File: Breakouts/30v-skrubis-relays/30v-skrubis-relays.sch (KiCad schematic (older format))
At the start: 13 parts, among them J1 Conn_01x03, J2 Conn_01x01, J4 Conn_01x01, J5 Conn_01x02, K1 G5Q-1A, Q1 Q_PNP_BEC, U1 PC817

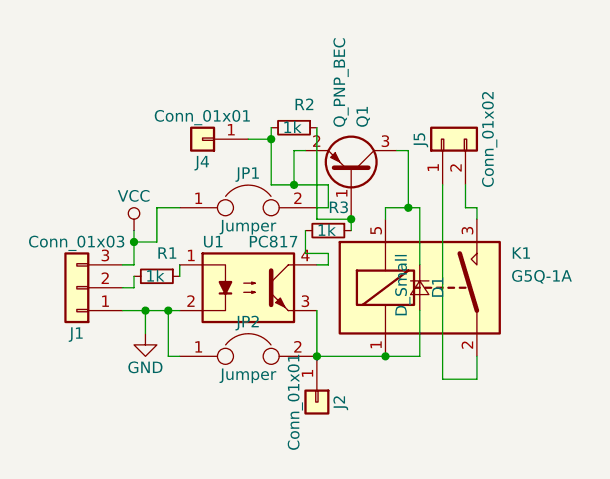
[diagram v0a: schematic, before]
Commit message: Changing the 48V relay breakout board so that all the SMD components are mounted on the bottom side => easier to assemble
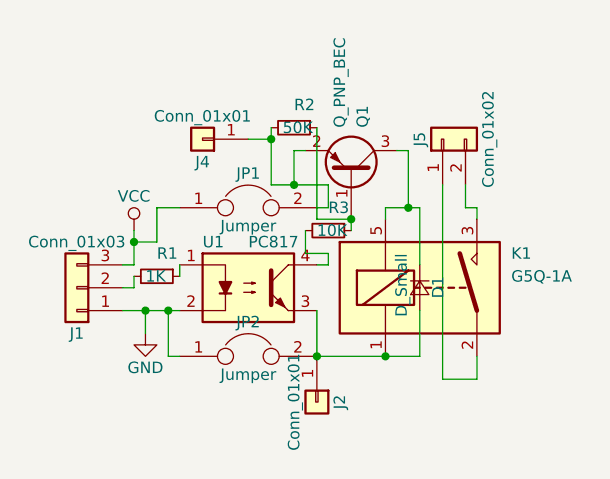
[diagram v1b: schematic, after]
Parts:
- R1: value 1k -> 1K
- R2: value 1k -> 50K
- R3: value 1k -> 10K
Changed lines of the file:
@@
-EESchema Schematic File Version 2
+EESchema Schematic File Version 4
 LIBS:power
-LIBS:device
-LIBS:switches
-LIBS:relays
-LIBS:motors
-LIBS:transistors
-LIBS:conn
-LIBS:linear
-LIBS:regul
 LIBS:74xx
-LIBS:cmos4000
-LIBS:adc-dac
-LIBS:memory
-LIBS:xilinx
-LIBS:microcontrollers
-LIBS:dsp
-LIBS:microchip
-LIBS:analog_switches
-LIBS:motorola
-LIBS:texas
-LIBS:intel
-LIBS:audio
-LIBS:interface
-LIBS:digital-audio
-LIBS:philips
-LIBS:display
-LIBS:cypress
-LIBS:siliconi
-LIBS:opto
-LIBS:atmel
-LIBS:contrib
-LIBS:valves
 LIBS:30v-skrubis-relays-cache
-EELAYER 25 0
+EELAYER 26 0
 EELAYER END
 $Descr A4 11693 8268
@@
 P 900 1300
 F 0 "R1" V 800 1300 50  0000 L CNN
-F 1 "1k" V 900 1250 50  0000 L CNN
+F 1 "1K" V 900 1250 50  0000 L CNN
 F 2 "Resistors_SMD:R_0603_HandSoldering" H 900 1300 50  0001 C CNN
 F 3 "" H 900 1300 50  0001 C CNN
@@
 	750  1250 800  1250
 Wire Wire Line
-	800  1250 800  1100
+	800  1250 800  1150
 Wire Wire Line
 	750  1350 800  1350
@@
 	1000 1300 1000 1250
 Wire Wire Line
-	750  1450 1000 1450
+	750  1450 850  1450
 $Comp
 L GND #PWR02
@@
 	1600 1450 1600 1650
 Wire Wire Line
-	1600 1650 2050 1650
+	1600 1650 1900 1650
 $Comp
 L Jumper JP1
@@
 	1300 700  1400 700
 Wire Wire Line
-	1400 650  1400 900
-Wire Wire Line
-	1400 900  1650 900
-Wire Wire Line
-	1900 1000 2050 1000
+	1400 650  1400 700
+Wire Wire Line
+	1400 900  1500 900
+Wire Wire Line
+	1900 1000 2000 1000
 $Comp
 L Q_PNP_BEC Q1
@@
 P 1650 1100
 F 0 "R3" V 1550 1100 50  0000 L CNN
-F 1 "1k" V 1650 1050 50  0000 L CNN
+F 1 "10K" V 1650 1050 50  0000 L CNN
 F 2 "Resistors_SMD:R_0603_HandSoldering" H 1650 1100 50  0001 C CNN
 F 3 "" H 1650 1100 50  0001 C CNN
@@
 P 1500 650
 F 0 "R2" V 1400 650 50  0000 L CNN
-F 1 "1k" V 1500 600 50  0000 L CNN
+F 1 "50K" V 1500 600 50  0000 L CNN
 F 2 "Resistors_SMD:R_0603_HandSoldering" H 1500 650 50  0001 C CNN
 F 3 "" H 1500 650 50  0001 C CNN
@@
 	1600 1050 1750 1050
 Connection ~ 1750 1050
+Wire Wire Line
+	850  1450 950  1450
+Wire Wire Line
+	950  1450 1000 1450
+Wire Wire Line
+	800  1150 800  1100
+Wire Wire Line
+	1900 1650 2050 1650
+Wire Wire Line
+	1500 900  1650 900
+Wire Wire Line
+	2000 1000 2050 1000
+Wire Wire Line
+	1400 700  1400 900
 $EndSCHEMATC
